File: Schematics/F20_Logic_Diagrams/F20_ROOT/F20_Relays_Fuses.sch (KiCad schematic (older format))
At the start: 23 parts, among them K1 MicroRelay, K2 MicroRelay, K3 MicroRelay, K4 MicroRelay, K5 MicroRelay

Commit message: Major powertrain update, added shifting schematic
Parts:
- removed F14: 1A, symbol FSAE_Library:Fuse
- added F?: 3A, symbol FSAE_Library:Fuse
- F13: value 30A -> FUSE
- F8: value 30A -> 15A
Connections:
- net SHIFT_PWR: now reaches F17.2
- new net ECU_+5V_2: F?.2
- new net ECU_+5V_Aux_Out2: F?.1
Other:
- note added: "* Driver Display (1A, 500mA min for stability)\n* Brake Pressure sensors (40mAx2 -> 100mA)"
- note added: "* Up/Down\n* Clutch"
- note added: "10A per Walbro"
- note removed: "* Driver Display (1A)\n* Brake Pressure sensors (40mAx2 -> 100mA)"
- note removed: "Recommended 1A supply (500mA min for stability)"
- moved on the sheet: F15, F16, F17, F18
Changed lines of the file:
@@
 $Descr A 11000 8500
 encoding utf-8
-Sheet 11 14
+Sheet 11 15
 Title "Relays and Fuses"
-Date "2020-01-29"
+Date "2020-03-04"
 Rev "A"
 Comp "F20"
@@
 P 3000 3750
 F 0 "F8" H 3300 3800 50  0000 C CNN
-F 1 "30A" H 3300 3700 50  0000 C CNN
+F 1 "15A" H 3300 3700 50  0000 C CNN
 F 2 "" H 3150 3830 50  0001 C CNN
 F 3 "~" V 3150 3900 50  0001 C CNN
@@
 P 3000 5750
 F 0 "F13" H 3300 5800 50  0000 C CNN
-F 1 "30A" H 3300 5700 50  0000 C CNN
+F 1 "FUSE" H 3300 5700 50  0000 C CNN
 F 2 "" H 3150 5830 50  0001 C CNN
 F 3 "~" V 3150 5900 50  0001 C CNN
@@
 	3300 5750 5000 5750
 $Comp
-L FSAE_Library:Fuse F14
-U 1 1 5E3E0FEB
-P 7000 5750
-F 0 "F14" H 7300 5800 50  0000 C CNN
-F 1 "1A" H 7300 5700 50  0000 C CNN
-F 2 "" H 7150 5830 50  0001 C CNN
-F 3 "~" V 7150 5900 50  0001 C CNN
-	1    7000 5750
-	1    0    0    -1
-$EndComp
-$Comp
 L FSAE_Library:Fuse F16
 U 1 1 5E3E18E2
-P 7000 6250
-F 0 "F16" H 7300 6300 50  0000 C CNN
-F 1 "1A" H 7300 6200 50  0000 C CNN
-F 2 "" H 7150 6330 50  0001 C CNN
-F 3 "~" V 7150 6400 50  0001 C CNN
-	1    7000 6250
+P 7000 6000
+F 0 "F16" H 7300 6050 50  0000 C CNN
+F 1 "1A" H 7300 5950 50  0000 C CNN
+F 2 "" H 7150 6080 50  0001 C CNN
+F 3 "~" V 7150 6150 50  0001 C CNN
+	1    7000 6000
 	1    0    0    -1
 $EndComp
@@
 Wire Wire Line
 	6500 6000 6500 5750
-Connection ~ 6500 5750
+Wire Wire Line
+	6500 6000 6500 6250
+Wire Wire Line
+	6500 6000 7000 6000
+Connection ~ 6500 6000
 Wire Wire Line
 	6500 5750 7000 5750
-Wire Wire Line
-	6500 6000 6500 6250
-Wire Wire Line
-	6500 6250 7000 6250
-Connection ~ 6500 6000
-Wire Wire Line
-	6500 6000 7000 6000
-Wire Wire Line
-	7300 5750 8000 5750
 Text GLabel 8000 5750 2    50   Output ~ 0
-DD_PWR
-Text GLabel 8000 6000 2    50   Output ~ 0
 RIM_PWR
 Wire Wire Line
-	8000 6000 7300 6000
+	8000 5750 7300 5750
 $Comp
 L FSAE_Library:Fuse F2
@@
 L FSAE_Library:Fuse F17
 U 1 1 5E3C06C7
-P 7000 6500
-F 0 "F17" H 7300 6550 50  0000 C CNN
-F 1 "Fuse" H 7300 6450 50  0000 C CNN
-F 2 "" H 7150 6580 50  0001 C CNN
-F 3 "~" V 7150 6650 50  0001 C CNN
-	1    7000 6500
+P 7000 6250
+F 0 "F17" H 7300 6300 50  0000 C CNN
+F 1 "Fuse" H 7300 6200 50  0000 C CNN
+F 2 "" H 7150 6330 50  0001 C CNN
+F 3 "~" V 7150 6400 50  0001 C CNN
+	1    7000 6250
 	1    0    0    -1
 $EndComp
@@
 Connection ~ 4500 5500
 Wire Wire Line
-	7300 6250 8000 6250
-Text GLabel 8000 6250 2    50   Output ~ 0
+	7300 6000 8000 6000
+Text GLabel 8000 6000 2    50   Output ~ 0
 TRANSPONDER_PWR
 Text GLabel 7000 2750 2    50   Output ~ 0
@@
 Text GLabel 8000 5000 2    50   Output ~ 0
 INJECTORS_PWR
-Text GLabel 3000 7000 0    50   Input ~ 0
+Text GLabel 3000 6500 0    50   Input ~ 0
 ECU_+5V_Aux_Out1
 $Comp
 L FSAE_Library:Fuse F18
 U 1 1 5E3EDD00
-P 3350 7000
-F 0 "F18" H 3650 7050 50  0000 C CNN
-F 1 "3A" H 3650 6950 50  0000 C CNN
-F 2 "" H 3500 7080 50  0001 C CNN
-F 3 "~" V 3500 7150 50  0001 C CNN
-	1    3350 7000
-	1    0    0    -1
-$EndComp
-Wire Wire Line
-	3350 7000 3000 7000
-Wire Wire Line
-	3650 7000 4000 7000
-Text GLabel 4000 7000 2    50   Output ~ 0
+P 3350 6500
+F 0 "F18" H 3650 6550 50  0000 C CNN
+F 1 "3A" H 3650 6450 50  0000 C CNN
+F 2 "" H 3500 6580 50  0001 C CNN
+F 3 "~" V 3500 6650 50  0001 C CNN
+	1    3350 6500
+	1    0    0    -1
+$EndComp
+Wire Wire Line
+	3350 6500 3000 6500
+Wire Wire Line
+	3650 6500 4000 6500
+Text GLabel 4000 6500 2    50   Output ~ 0
 ECU_+5V_1
 Wire Wire Line
@@
 ECU_+12V_IGN
 Wire Wire Line
-	7000 6500 6500 6500
-Wire Wire Line
-	6500 6500 6500 6250
-Connection ~ 6500 6250
-Text Notes 8400 6100 0    50   ~ 0
+	7000 6250 6500 6250
+Text Notes 8400 5850 0    50   ~ 0
 KA7805 voltage regulator (1A)
 $Comp
 L FSAE_Library:Fuse F15
 U 1 1 5E3E15AD
-P 7000 6000
-F 0 "F15" H 7300 6050 50  0000 C CNN
-F 1 "1A" H 7300 5950 50  0000 C CNN
-F 2 "" H 7150 6080 50  0001 C CNN
-F 3 "~" V 7150 6150 50  0001 C CNN
-	1    7000 6000
-	1    0    0    -1
-$EndComp
-Text Notes 8400 5800 0    50   ~ 0
-Recommended 1A supply (500mA min for stability)
+P 7000 5750
+F 0 "F15" H 7300 5800 50  0000 C CNN
+F 1 "1A" H 7300 5700 50  0000 C CNN
+F 2 "" H 7150 5830 50  0001 C CNN
+F 3 "~" V 7150 5900 50  0001 C CNN
+	1    7000 5750
+	1    0    0    -1
+$EndComp
 Text Notes 8650 2600 0    50   ~ 0
 MUST KILL IGNITION AND\nFUEL PER FSAE RULES
-Text Notes 8800 6300 0    50   ~ 0
+Text Notes 8800 6050 0    50   ~ 0
 about 60mA
-Text Notes 3450 7300 0    50   ~ 10
-* Driver Display (1A)\n* Brake Pressure sensors (40mAx2 -> 100mA)
+Text Notes 3450 6800 0    50   ~ 0
+* Driver Display (1A, 500mA min for stability)\n* Brake Pressure sensors (40mAx2 -> 100mA)
 Wire Wire Line
 	7000 2500 7500 2500
 Wire Wire Line
 	8000 2500 8500 2500
+Text GLabel 3000 7000 0    50   Input ~ 0
+ECU_+5V_Aux_Out2
+$Comp
+L FSAE_Library:Fuse F?
+U 1 1 5E60DDBF
+P 3350 7000
+F 0 "F?" H 3650 7050 50  0000 C CNN
+F 1 "3A" H 3650 6950 50  0000 C CNN
+F 2 "" H 3500 7080 50  0001 C CNN
+F 3 "~" V 3500 7150 50  0001 C CNN
+	1    3350 7000
+	1    0    0    -1
+$EndComp
+Wire Wire Line
+	3350 7000 3000 7000
+Wire Wire Line
+	3650 7000 4000 7000
+Text GLabel 4000 7000 2    50   Output ~ 0
+ECU_+5V_2
+Text Notes 7700 3800 0    50   ~ 0
+10A per Walbro
+Connection ~ 6500 5750
+Text GLabel 8000 6250 2    50   Output ~ 0
+SHIFT_PWR
+Wire Wire Line
+	8000 6250 7300 6250
+Text Notes 8500 6350 0    50   ~ 0
+* Up/Down\n* Clutch
 $EndSCHEMATC

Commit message: Update
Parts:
- removed F10, F11: Fuse, symbol FSAE_Library:Fuse
- F13: value FUSE -> 10A
- F15: value 1A -> 2A
- F17: value Fuse -> 5A
- F8: value 15A -> 20A
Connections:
- net COILS_PWR: now also K4.5
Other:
- note added: "* Up/Down 0.832A\n* Clutch 1.625A\nTotal = 2.457A"
- note added: "4*3=12A"
- note added: "Don't think fuse is required\nbetween relay and these two\noutputs. CHECK!!"
- note removed: "* Up/Down\n* Clutch"
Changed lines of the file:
@@
 EESchema Schematic File Version 4
-LIBS:F20_ROOT-cache
 EELAYER 30 0
 EELAYER END
@@
 P 3000 3750
 F 0 "F8" H 3300 3800 50  0000 C CNN
-F 1 "15A" H 3300 3700 50  0000 C CNN
+F 1 "20A" H 3300 3700 50  0000 C CNN
 F 2 "" H 3150 3830 50  0001 C CNN
 F 3 "~" V 3150 3900 50  0001 C CNN
@@
 P 3000 5750
 F 0 "F13" H 3300 5800 50  0000 C CNN
-F 1 "FUSE" H 3300 5700 50  0000 C CNN
+F 1 "10A" H 3300 5700 50  0000 C CNN
 F 2 "" H 3150 5830 50  0001 C CNN
 F 3 "~" V 3150 5900 50  0001 C CNN
@@
 Wire Wire Line
 	6000 5500 5600 5500
-$Comp
-L FSAE_Library:Fuse F11
-U 1 1 5E3A862B
-P 7000 5000
-F 0 "F11" H 7300 5050 50  0000 C CNN
-F 1 "Fuse" H 7300 4950 50  0000 C CNN
-F 2 "" H 7150 5080 50  0001 C CNN
-F 3 "~" V 7150 5150 50  0001 C CNN
-	1    7000 5000
-	1    0    0    -1
-$EndComp
 Wire Wire Line
 	6500 4750 6500 5000
-Wire Wire Line
-	6500 5000 7000 5000
-Wire Wire Line
-	7300 5000 8000 5000
 Text GLabel 8000 2000 2    50   Output ~ 0
 O2_SNSR_PWR
@@
 P 7000 6250
 F 0 "F17" H 7300 6300 50  0000 C CNN
-F 1 "Fuse" H 7300 6200 50  0000 C CNN
+F 1 "5A" H 7300 6200 50  0000 C CNN
 F 2 "" H 7150 6330 50  0001 C CNN
 F 3 "~" V 7150 6400 50  0001 C CNN
@@
 Text GLabel 7000 2750 2    50   Output ~ 0
 FAN_PWR
-$Comp
-L FSAE_Library:Fuse F10
-U 1 1 5E3E67D5
-P 7000 4750
-F 0 "F10" H 7300 4800 50  0000 C CNN
-F 1 "Fuse" H 7300 4700 50  0000 C CNN
-F 2 "" H 7150 4830 50  0001 C CNN
-F 3 "~" V 7150 4900 50  0001 C CNN
-	1    7000 4750
-	1    0    0    -1
-$EndComp
-Wire Wire Line
-	6500 4750 7000 4750
 Connection ~ 6500 4750
-Wire Wire Line
-	7300 4750 8000 4750
 Text GLabel 8000 4750 2    50   Output ~ 0
 COILS_PWR
@@
 P 7000 5750
 F 0 "F15" H 7300 5800 50  0000 C CNN
-F 1 "1A" H 7300 5700 50  0000 C CNN
+F 1 "2A" H 7300 5700 50  0000 C CNN
 F 2 "" H 7150 5830 50  0001 C CNN
 F 3 "~" V 7150 5900 50  0001 C CNN
@@
 Wire Wire Line
 	8000 6250 7300 6250
-Text Notes 8500 6350 0    50   ~ 0
-* Up/Down\n* Clutch
+Text Notes 8500 6400 0    50   ~ 0
+* Up/Down 0.832A\n* Clutch 1.625A\nTotal = 2.457A
+Wire Wire Line
+	6500 4750 8000 4750
+Wire Wire Line
+	6500 5000 8000 5000
+Text Notes 8700 5050 0    50   ~ 0
+4*3=12A
+Text Notes 9050 4950 0    50   ~ 0
+Don't think fuse is required\nbetween relay and these two\noutputs.  CHECK!!
 $EndSCHEMATC

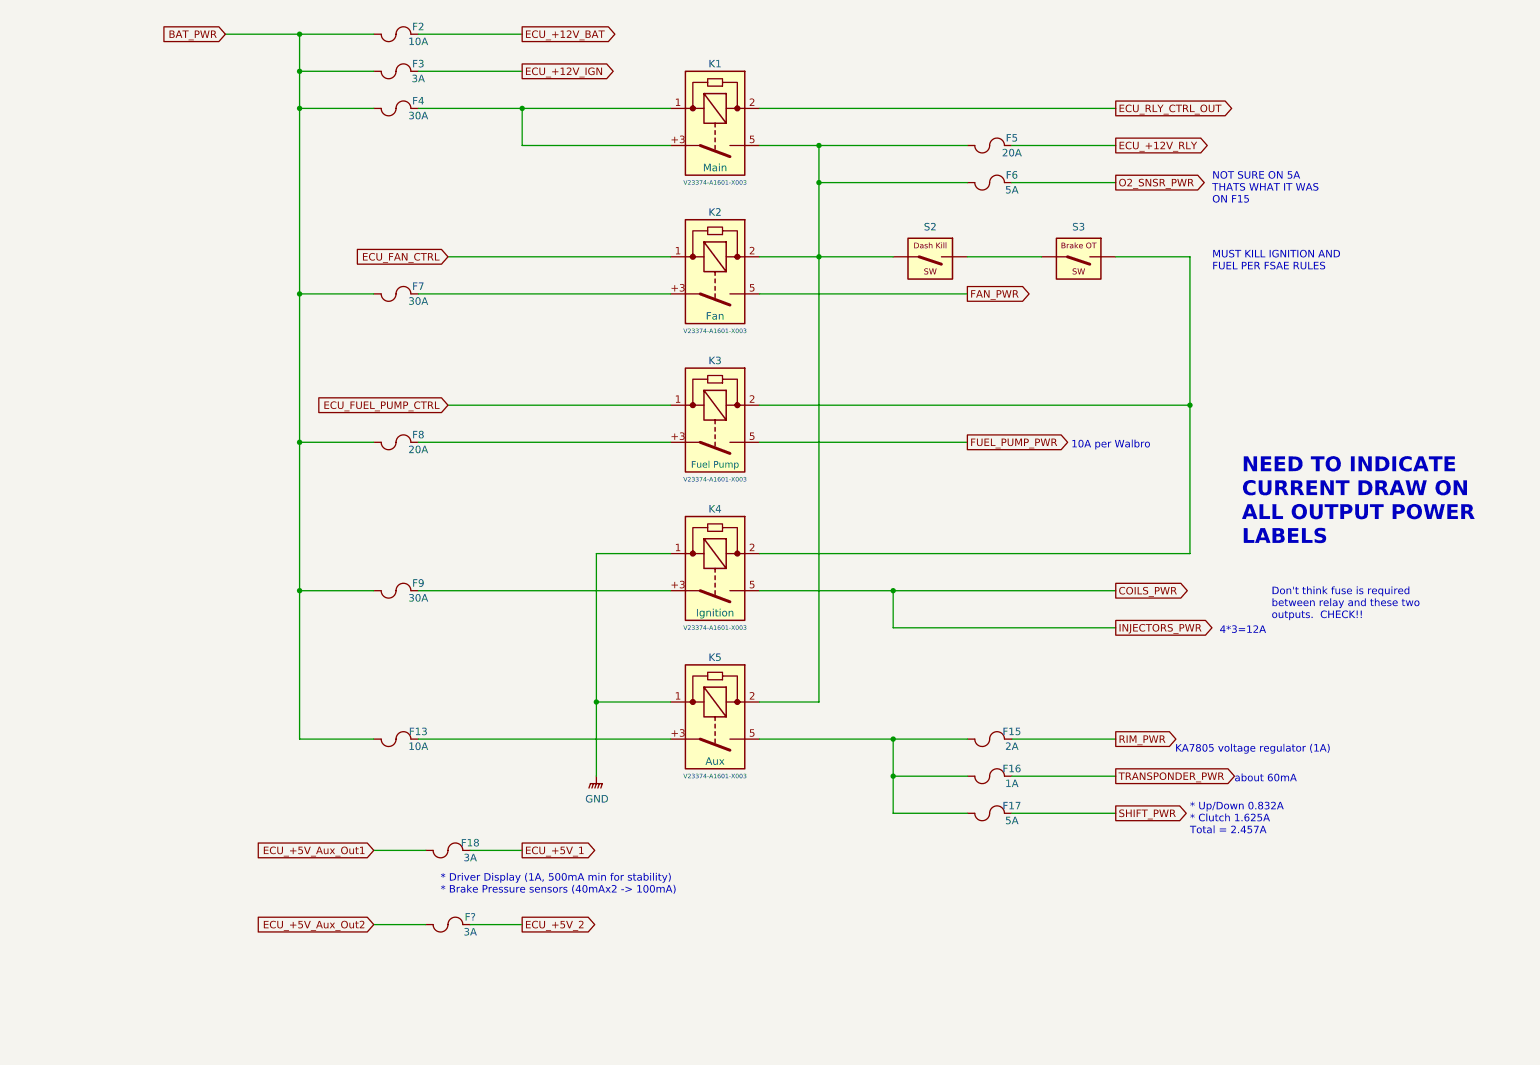
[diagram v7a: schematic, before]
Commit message: Added steering wheel drawing, udpated some ECU pinout to match previous tune, added accel/XBEE drawing
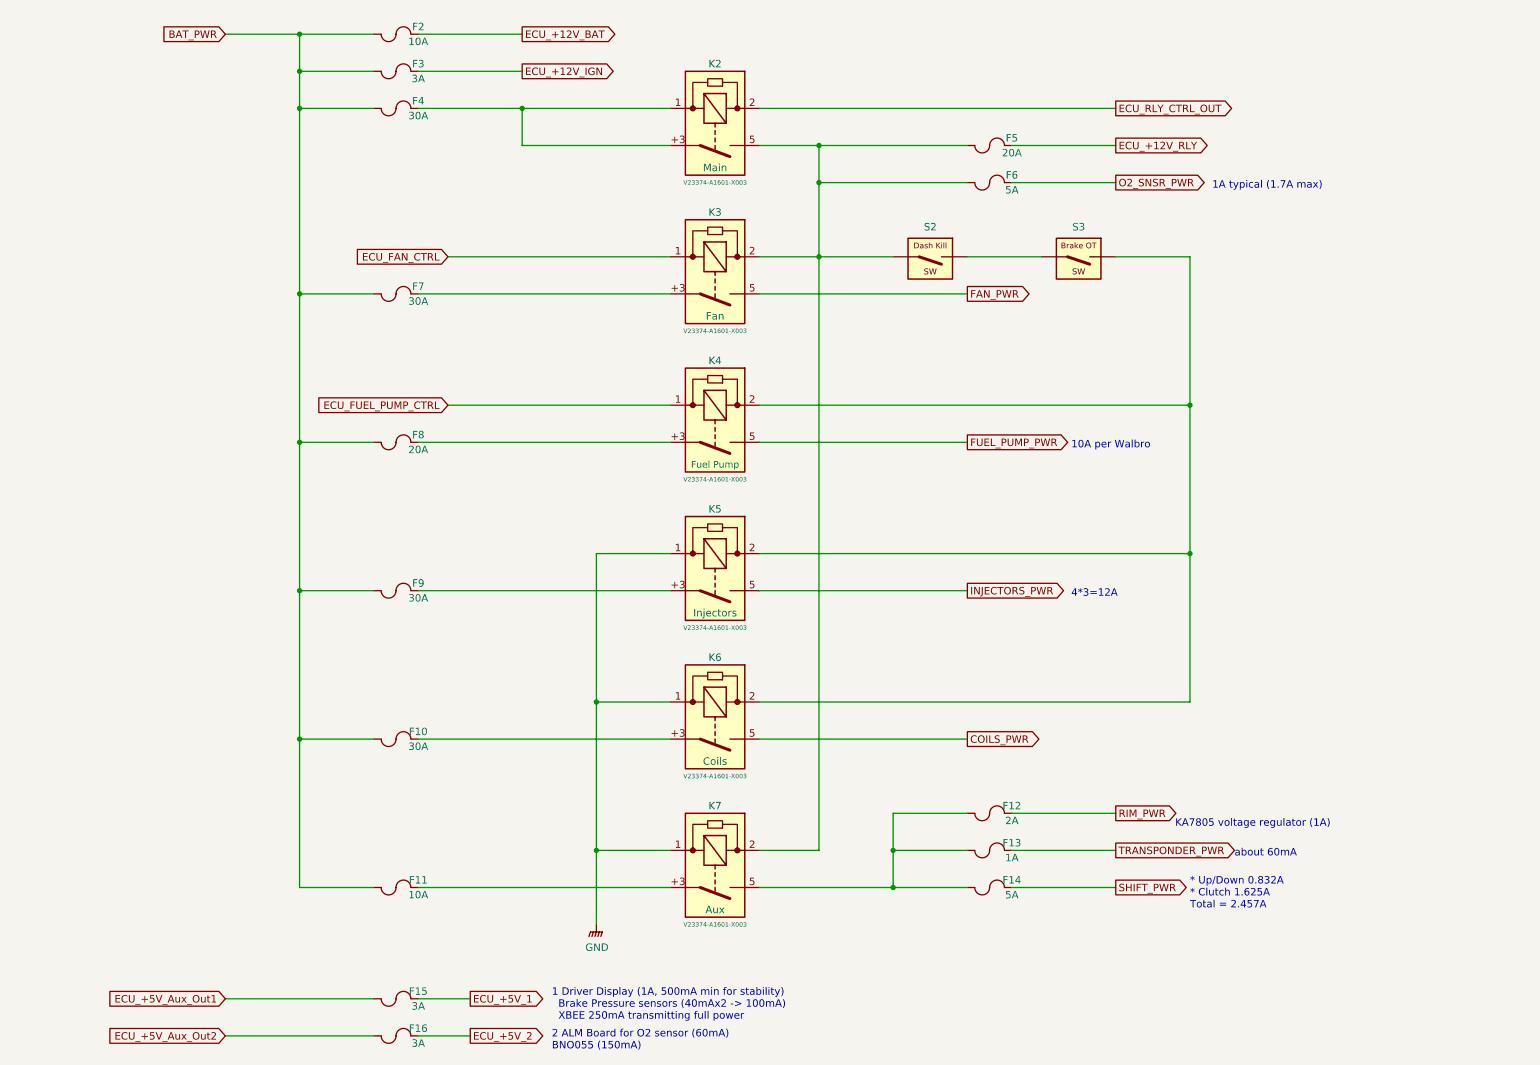
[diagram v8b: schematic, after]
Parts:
- added F10: 30A, symbol FSAE_Library:Fuse
- added K6: MicroRelay, symbol FSAE_Library:MicroRelay
- K5: renamed from K4; Name Ignition -> Injectors
- gave numbers to parts that had none: 1
- renumbered F13 to F11, F15 to F12, F16 to F13, F17 to F14, F18 to F15, K1 to K2, K2 to K3, K3 to K4, K5 to K7
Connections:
- net BAT_PWR: now also F10.1
- net COILS_PWR: now also K6.5; no longer K5.5
- net GNDPWR: now also K6.1
- net at K4.2, K5.2, S3.~: now also K6.2
- new net: F10.2, K6.+3
- new net INJECTORS_PWR: K5.5
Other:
- note added: "1 Driver Display (1A, 500mA min for stability)\n Brake Pressure sensors (40mAx2 -> 100mA)\n XBEE 250mA transmitting full power"
- note added: "1A typical (1.7A max)"
- note added: "2 ALM Board for O2 sensor (60mA)\nBNO055 (150mA)"
- note removed: "* Driver Display (1A, 500mA min for stability)\n* Brake Pressure sensors (40mAx2 -> 100mA)"
- note removed: "Don't think fuse is required\nbetween relay and these two\noutputs. CHECK!!"
- note removed: "MUST KILL IGNITION AND\nFUEL PER FSAE RULES"
- note removed: "NEED TO INDICATE\nCURRENT DRAW ON\nALL OUTPUT POWER\nLABELS"
- note removed: "NOT SURE ON 5A\nTHATS WHAT IT WAS\nON F15"
- moved on the sheet: F11, F12, F13, F14, F15, F16, K7
